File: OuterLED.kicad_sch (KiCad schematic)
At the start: 2 parts

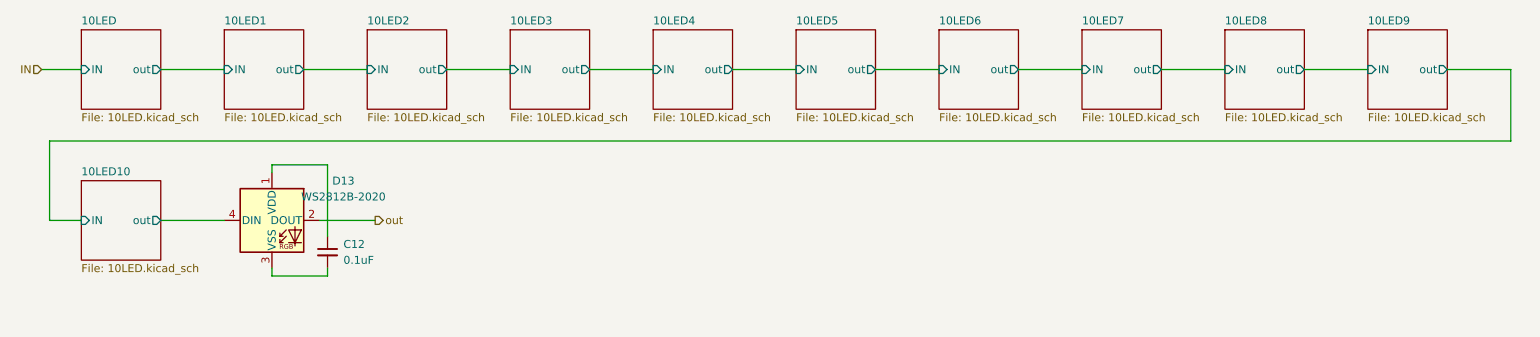
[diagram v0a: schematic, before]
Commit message: 外周LEDを116個に修正
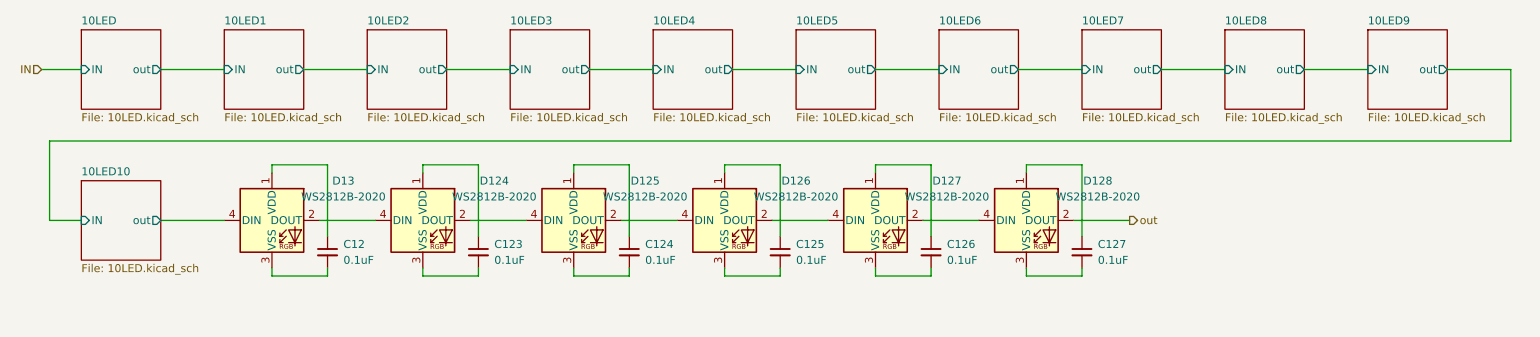
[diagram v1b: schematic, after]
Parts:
- added C123, C124, C125, C126, C127: 0.1uF, symbol Device:C_Small
- added D124, D125, D126, D127, D128: WS2812B-2020, LED_SMD:LED_WS2812B_PLCC4_5.0x5.0mm_P3.2mm, symbol LED:WS2812B
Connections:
- net out: now also D128.2 (DOUT); no longer D13.2 (DOUT)
- new net: C126.1, D127.1 (VDD)
- new net: D127.2 (DOUT), D128.4 (DIN)
- new net: C126.2, D127.3 (VSS)
- new net: D126.2 (DOUT), D127.4 (DIN)
- new net: C124.1, D125.1 (VDD)
- new net: D125.2 (DOUT), D126.4 (DIN)
- new net: C124.2, D125.3 (VSS)
- new net: D124.2 (DOUT), D125.4 (DIN)
- new net: C127.1, D128.1 (VDD)
- new net: C127.2, D128.3 (VSS)
- new net: C125.1, D126.1 (VDD)
- new net: C125.2, D126.3 (VSS)
- new net: C123.1, D124.1 (VDD)
- new net: C123.2, D124.3 (VSS)
- new net: D124.4 (DIN), D13.2 (DOUT)

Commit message: 部品修正
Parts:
- D124, D125, D126, D127, D128, D13: footprint LED_SMD:LED_WS2812B_PLCC4_5.0x5.0mm_P3.2mm -> LED_SMD:LED_WS2812B-2020_PLCC4_2.0x2.0mm; symbol LED:WS2812B -> LED:WS2812B-2020
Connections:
- net 10LED10/out: now also D13.3 (DIN); no longer D13.4 (DIN)
- net out: now also D128.1 (DOUT); no longer D128.2 (DOUT)
- net at D127.1 (DOUT): now also D128.3 (DIN); no longer C126.1
- net +5V: now reaches D128.4 (VDD)
- net +5V: now also C12.1, C123.1, C124.1, C125.1, C126.1, C127.1, D124.4 (VDD), D125.4 (VDD), D126.4 (VDD), D127.4 (VDD), D13.4 (VDD); no longer D127.2 (DOUT)
- net at D127.3 (DIN): now also D126.1 (DOUT); no longer C126.2
- net GND: now reaches D126.2 (VSS)
- net GND: now also C12.2, C123.2, C124.2, C125.2, C126.2, C127.2, D124.2 (VSS), D125.2 (VSS), D127.2 (VSS), D128.2 (VSS), D13.2 (VSS); no longer D127.4 (DIN)
- net at D125.1 (DOUT): now also D126.3 (DIN); no longer C124.1
- net at D125.3 (DIN): now also D124.1 (DOUT); no longer C124.2
- net at D124.3 (DIN): now also D13.1 (DOUT); no longer C123.2
